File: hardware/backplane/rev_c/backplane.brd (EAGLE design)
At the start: 254 x 381 mm, 379 parts, among them J0 BACKPLANE_GENERIC_MODULE, J1 BACKPLANE_GENERIC_MODULE, J2 BACKPLANE_GENERIC_MODULE, J3 BACKPLANE_CONTROLLER_MODULE, J4 BACKPLANE_POWER_MODULE, J5 BACKPLANE_GENERIC_MODULE, J6 BACKPLANE_GENERIC_MODULE, J7 BACKPLANE_GENERIC_MODULE, U1 TUSB2077A, U10 SN74LVC2T45, U11 SN74LVC2T45, U12 SN74LVC2T45, U13 SN74LVC2T45, U14 SN74LVC2T45, U15 SN74LVC2T45, U16 SN74LVC2T45, U17 SN74LVC2T45, U18 SN74LVC2T45, U19 SN74LVC2T45, U2 FXMA2102, U20 TS3USB30E, U21 TS3USB30E, U22 TS3USB30E, U23 TS3USB30E, U24 TS3USB30E, U25 TS3USB30E, U26 MCP23008QFN, U27 MCP23008QFN, U28 MCP23008QFN, U29 MCP23008QFN, U3 FXMA2102, U30 MCP23008QFN, U31 MCP23008QFN, U32 MCP23008QFN, U4 FXMA2102, U5 FXMA2102, U6 FXMA2102, U7 FXMA2102, U8 SN74LVC2T45, U9 SN74LVC2T45, Y1 ABMM

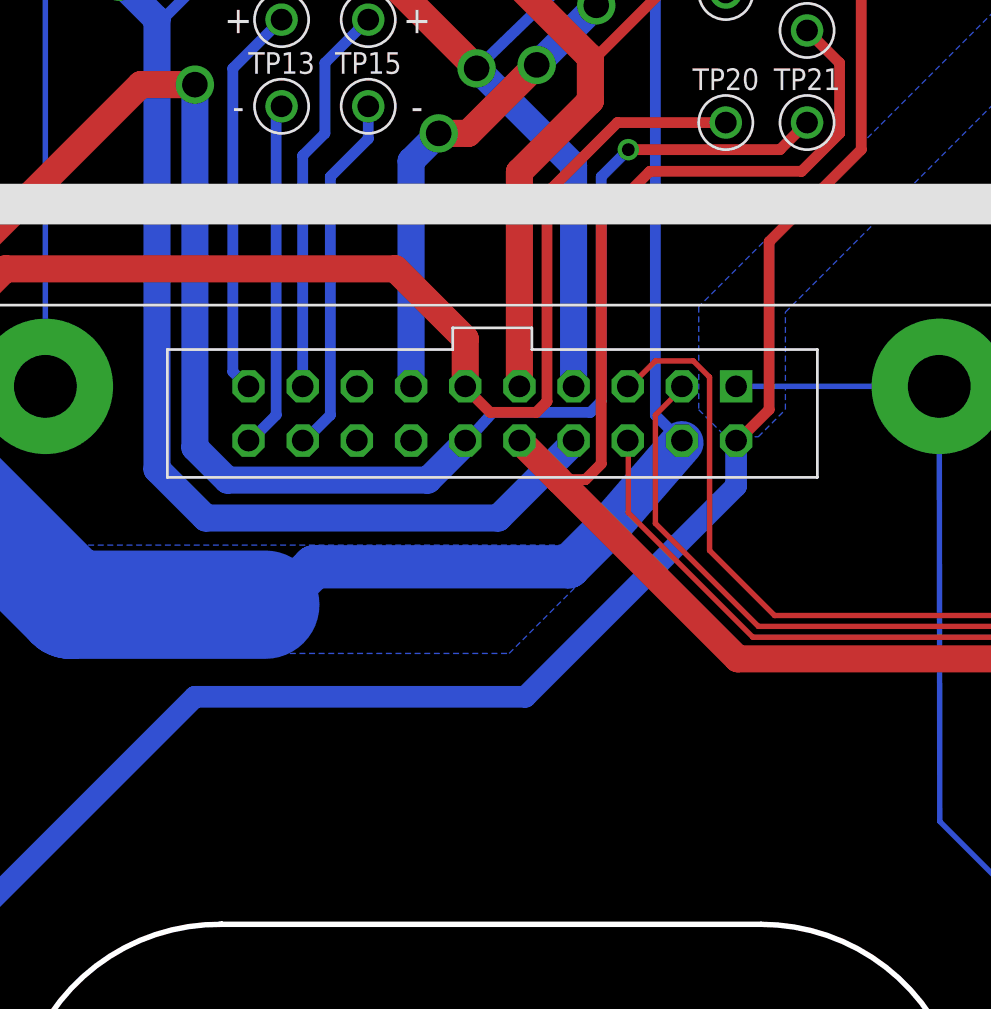
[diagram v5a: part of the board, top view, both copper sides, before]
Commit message: added terminal blocks to backplane
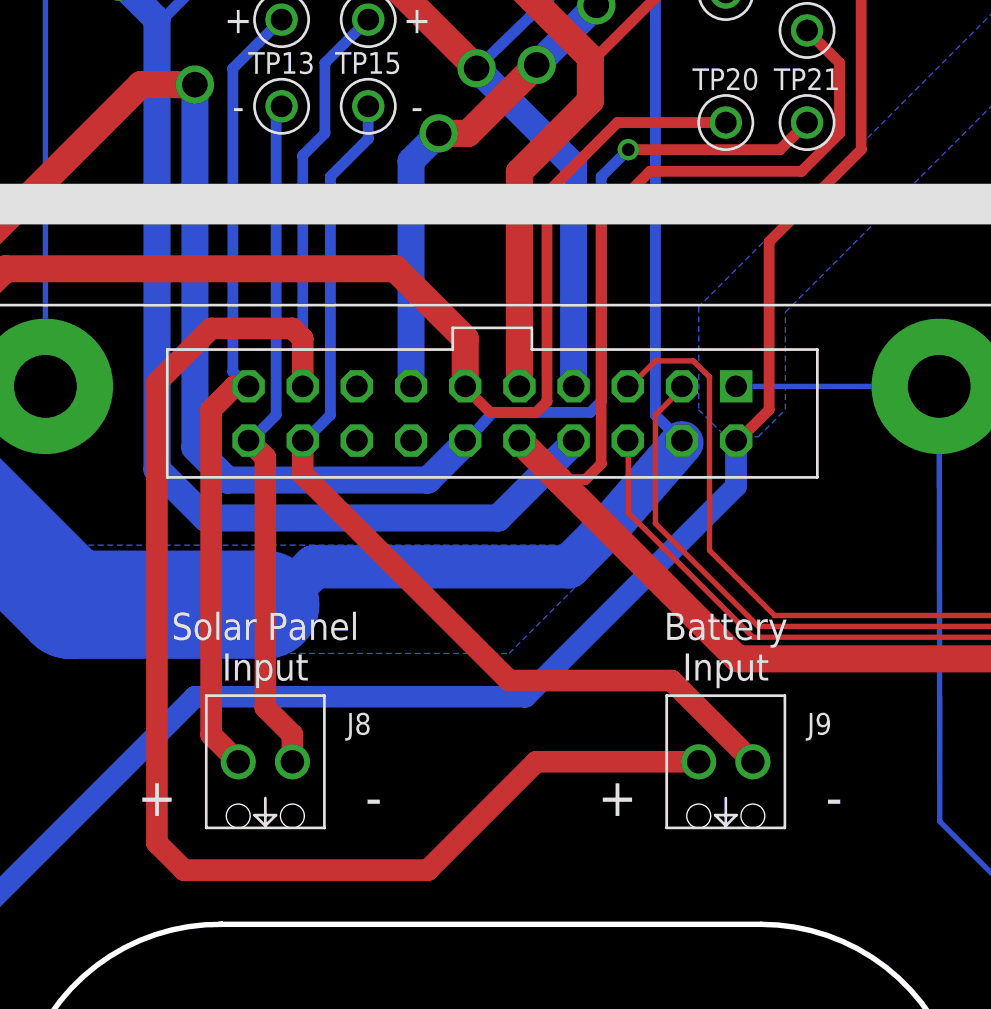
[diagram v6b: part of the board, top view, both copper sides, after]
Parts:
- added J8, J9: SCREW-TERMINAL_2_0.100, headers:CONN_BLOCK_2
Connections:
- net VBATT+: now also J9.1
- net VBATT-: now also J9.2
- net VSOL+: now also J8.1
- net VSOL-: now also J8.2
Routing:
- net VBATT+: track 18.5 -> 78.4 mm
- net VBATT-: track 17.0 -> 45.3 mm
- net VSOL+: track 18.5 -> 37.7 mm
- net VSOL-: track 16.4 -> 32.3 mm
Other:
- board text added: "Battery Input"
- board text added: "Solar Panel Input"
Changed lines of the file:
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@@
 <?xml version="1.0" encoding="utf-8"?>
 <!DOCTYPE eagle SYSTEM "eagle.dtd">
-<eagle version="6.6.0">
+<eagle version="8.0.2">
 <drawing>
 <settings>
@@
 <setting verticaltext="up"/>
 </settings>
-<grid distance="0.005" unitdist="inch" unit="inch" style="lines" multiple="1" display="yes" altdistance="0.01" altunitdist="inch" altunit="inch"/>
+<grid distance="0.05" unitdist="inch" unit="inch" style="lines" multiple="1" display="yes" altdistance="0.01" altunitdist="inch" altunit="inch"/>
 <layers>
 <layer number="1" name="Top" color="4" fill="1" visible="yes" active="yes"/>
@@
 <wire x1="33.401" y1="127" x2="33.528" y2="146.05" width="0.254" layer="20" curve="-180.763898"/>
 <wire x1="58.801" y1="146.05" x2="58.801" y2="127" width="0.254" layer="20" curve="-180"/>
+<text x="35.56" y="157.48" size="1.27" layer="21" font="vector" ratio="12" align="bottom-center">Solar Panel
+Input</text>
+<text x="57.15" y="157.48" size="1.27" layer="21" font="vector" ratio="12" align="bottom-center">Battery
+Input</text>
+<text x="40.64" y="151.13" size="1.778" layer="21" font="vector" ratio="12" align="bottom-center">-</text>
+<text x="30.48" y="151.13" size="1.778" layer="21" font="vector" ratio="12" align="bottom-center">+</text>
+<text x="52.07" y="151.13" size="1.778" layer="21" font="vector" ratio="12" align="bottom-center">+</text>
+<text x="62.23" y="151.13" size="1.778" layer="21" font="vector" ratio="12" align="bottom-center">-</text>
 </plain>
 <attributes>
@@
 <pass name="Default">
 <param name="RoutingGrid" value="50mil"/>
+<param name="AutoGrid" value="1"/>
+<param name="Efforts" value="0"/>
+<param name="TopRouterVariant" value="1"/>
 <param name="tpViaShape" value="round"/>
 <param name="PrefDir.1" value="|"/>
@@
 <attribute name="VALUE" x="164.084" y="79.248" size="1.27" layer="27" rot="R90"/>
 </element>
+<element name="J8" library="headers" package="CONN_BLOCK_2" value="SCREW-TERMINAL_2_0.100" x="35.56" y="153.67" smashed="yes">
+<attribute name="DIGIKEY" value="277-1273-ND" x="35.56" y="153.67" size="1.778" layer="27" font="vector" ratio="12" display="off"/>
+<attribute name="MOUSER" value="651-1725656" x="35.56" y="153.67" size="1.778" layer="27" font="vector" ratio="12" display="off"/>
+<attribute name="NAME" x="39.37" y="154.94" size="1.016" layer="25" font="vector" ratio="12"/>
+<attribute name="NEWARK" value="71C4107" x="35.56" y="153.67" size="1.778" layer="27" font="vector" ratio="12" display="off"/>
+</element>
+<element name="J9" library="headers" package="CONN_BLOCK_2" value="SCREW-TERMINAL_2_0.100" x="57.15" y="153.67" smashed="yes">
+<attribute name="DIGIKEY" value="277-1273-ND" x="57.15" y="153.67" size="1.778" layer="27" font="vector" ratio="12" display="off"/>
+<attribute name="MOUSER" value="651-1725656" x="57.15" y="153.67" size="1.778" layer="27" font="vector" ratio="12" display="off"/>
+<attribute name="NAME" x="60.96" y="154.94" size="1.016" layer="25" font="vector" ratio="12"/>
+<attribute name="NEWARK" value="71C4107" x="57.15" y="153.67" size="1.778" layer="27" font="vector" ratio="12" display="off"/>
+</element>
 </elements>
 <signals>
@@
 <wire x1="34.036" y1="171.958" x2="34.036" y2="186.182" width="0.508" layer="16"/>
 <wire x1="34.036" y1="186.182" x2="36.322" y2="188.468" width="0.508" layer="16"/>
+<contactref element="J8" pad="1"/>
+<wire x1="34.7726" y1="171.2722" x2="34.1122" y2="171.2722" width="1.016" layer="1"/>
+<wire x1="34.1122" y1="171.2722" x2="33.02" y2="170.18" width="1.016" layer="1"/>
+<wire x1="33.02" y1="170.18" x2="33.02" y2="154.94" width="1.016" layer="1"/>
+<wire x1="33.02" y1="154.94" x2="34.29" y2="153.67" width="1.016" layer="1"/>
 </signal>
 <signal name="VSOL-">
@@
 <wire x1="36.068" y1="169.926" x2="36.068" y2="184.15" width="0.508" layer="16"/>
 <wire x1="36.068" y1="184.15" x2="36.322" y2="184.404" width="0.508" layer="16"/>
+<contactref element="J8" pad="2"/>
+<wire x1="36.83" y1="153.67" x2="36.83" y2="154.94" width="1.016" layer="1"/>
+<wire x1="36.83" y1="154.94" x2="35.56" y2="156.21" width="1.016" layer="1"/>
+<wire x1="35.56" y1="156.21" x2="35.56" y2="167.9448" width="1.016" layer="1"/>
+<wire x1="35.56" y1="167.9448" x2="34.7726" y2="168.7322" width="1.016" layer="1"/>
 </signal>
 <signal name="VBATT+">
-<contactref element="J4" pad="17"/>
 <contactref element="TP14" pad="TESTPOINT"/>
-<wire x1="37.3126" y1="171.2722" x2="37.3126" y2="182.0926" width="0.508" layer="16"/>
-<wire x1="37.3126" y1="182.0926" x2="38.354" y2="183.134" width="0.508" layer="16"/>
+<wire x1="38.354" y1="183.134" x2="37.3126" y2="182.0926" width="0.508" layer="16"/>
 <wire x1="38.354" y1="183.134" x2="38.354" y2="186.436" width="0.508" layer="16"/>
 <wire x1="38.354" y1="186.436" x2="40.386" y2="188.468" width="0.508" layer="16"/>
+<contactref element="J4" pad="17"/>
+<contactref element="J9" pad="1"/>
+<wire x1="37.3126" y1="171.2722" x2="37.3126" y2="173.5074" width="1.016" layer="1"/>
+<wire x1="37.3126" y1="173.5074" x2="36.83" y2="173.99" width="1.016" layer="1"/>
+<wire x1="36.83" y1="173.99" x2="33.02" y2="173.99" width="1.016" layer="1"/>
+<wire x1="33.02" y1="173.99" x2="30.48" y2="171.45" width="1.016" layer="1"/>
+<wire x1="30.48" y1="171.45" x2="30.48" y2="149.86" width="1.016" layer="1"/>
+<wire x1="30.48" y1="149.86" x2="31.75" y2="148.59" width="1.016" layer="1"/>
+<wire x1="31.75" y1="148.59" x2="43.18" y2="148.59" width="1.016" layer="1"/>
+<wire x1="37.3126" y1="182.0926" x2="37.3126" y2="171.2722" width="0.508" layer="16"/>
+<wire x1="43.18" y1="148.59" x2="48.26" y2="153.67" width="1.016" layer="1"/>
+<wire x1="48.26" y1="153.67" x2="55.88" y2="153.67" width="1.016" layer="1"/>
 </signal>
 <signal name="VBATT-">
-<contactref element="J4" pad="18"/>
 <contactref element="TP15" pad="TESTPOINT"/>
-<wire x1="37.3126" y1="168.7322" x2="37.4142" y2="168.7322" width="0.508" layer="16"/>
-<wire x1="37.4142" y1="168.7322" x2="38.608" y2="169.926" width="0.508" layer="16"/>
-<wire x1="38.608" y1="169.926" x2="38.608" y2="181.102" width="0.508" layer="16"/>
+<wire x1="38.608" y1="181.102" x2="38.608" y2="169.926" width="0.508" layer="16"/>
 <wire x1="38.608" y1="181.102" x2="40.386" y2="182.88" width="0.508" layer="16"/>
 <wire x1="40.386" y1="182.88" x2="40.386" y2="184.404" width="0.508" layer="16"/>
+<contactref element="J4" pad="18"/>
+<contactref element="J9" pad="2"/>
+<wire x1="37.3126" y1="168.7322" x2="37.3126" y2="167.1574" width="1.016" layer="1"/>
+<wire x1="37.3126" y1="167.1574" x2="46.99" y2="157.48" width="1.016" layer="1"/>
+<wire x1="46.99" y1="157.48" x2="54.61" y2="157.48" width="1.016" layer="1"/>
+<wire x1="54.61" y1="157.48" x2="58.42" y2="153.67" width="1.016" layer="1"/>
+<wire x1="38.608" y1="169.926" x2="37.4142" y2="168.7322" width="0.508" layer="16"/>
+<wire x1="37.4142" y1="168.7322" x2="37.3126" y2="168.7322" width="0.508" layer="16"/>
 </signal>
 <signal name="HUB_DP1">

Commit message: backplane: use #4 holes
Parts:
- removed H1, H10, H11, H12, H13, H14, H15, H16, H17, H18, H19, H2, H20, H3, H4, H5, H6, H7, H8, H9: MOUNT-PAD-ROUND3.0, holes:3,0-PAD
- added H21, H22, H23, H24, H25, H26, H27, H28, H29, H30, H31, H32, H33, H34, H35, H36, H37, H38, H39, H40: MOUNT-PAD-ROUND#4, holes:#4-PAD
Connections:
- net GND: now also H21.B#4, H22.B#4, H23.B#4, H24.B#4, H25.B#4, H26.B#4, H27.B#4, H28.B#4, H29.B#4, H30.B#4, H31.B#4, H32.B#4, H33.B#4, H34.B#4, H35.B#4, H36.B#4, H37.B#4, H38.B#4, H39.B#4, H40.B#4; no longer H1.B3,0, H10.B3,0, H11.B3,0, H12.B3,0, H13.B3,0, H14.B3,0, H15.B3,0, H16.B3,0, H17.B3,0, H18.B3,0, H19.B3,0, H2.B3,0, H20.B3,0, H3.B3,0, H4.B3,0, H5.B3,0, H6.B3,0, H7.B3,0, H8.B3,0, H9.B3,0
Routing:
- net GND: track 2946.4 -> 2940.9 mm
